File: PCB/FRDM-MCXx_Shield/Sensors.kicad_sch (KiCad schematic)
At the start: 3 parts, among them IC1 FXLS8974CF, J1 Conn_01x05_Socket

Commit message: Updated schematic
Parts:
- removed IC1: FXLS8974CF, FXLS8974CF, symbol SamacSys_Parts:FXLS8974CF
- added C10, C12, C8: 100nF, Capacitor_SMD:C_0603_1608Metric_Pad1.08x0.95mm_HandSolder, symbol Device:C
- added C11: 1uF, Capacitor_SMD:C_0603_1608Metric_Pad1.08x0.95mm_HandSolder, symbol Device:C
- added RN2: 4.7k, Resistor_SMD:R_Array_Convex_4x0603, symbol Device:R_Pack04_Split
- added U4: FXLS8974CF, FXLS8974CF, symbol SamacSys_Parts:FXLS8974CF
- added U5: SHT31A-DIS, Sensor_Humidity:Sensirion_DFN-8-1EP_2.5x2.5mm_P0.5mm_EP1.1x1.7mm, symbol Sensor_Humidity:SHT31A-DIS
- J1: footprint (none) -> Connector_PinHeader_2.54mm:PinHeader_1x05_P2.54mm_Vertical
- RV1: value R_Potentiometer -> 5k; footprint (none) -> Potentiometer_THT:Potentiometer_Vishay_T73YP_Vertical
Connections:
- net +3.3V: now also RV1.1, C10.1, C11.1, C12.2, C8.1, RN2.7 (R2.2), RN2.8 (R1.2), U4.1 (VDD), U4.9 (INTF_SEL), U5.5 (VDD)
- net GND: now also RV1.3, C10.2, C11.2, C12.1, C8.2, U4.10 (GND), U4.2 (BT_MODE), U5.2 (ADDR), U5.7 (R), U5.8 (VSS), U5.9 (VSS)
- net ADC_OUT: now reaches RV1.2
- new net ACEL_CS: U4.7 (SPI_CS_B/WAKE_UP)
- new net ACEL_INT1: RN2.1 (R1.1), U4.8 (INT1/MOT_DET)
- new net ACEL_INT2: RN2.2 (R2.1), U4.6 (INT2/EXT_TRIG/BOOT_OUT)
- new net SCL: U5.4 (SCL)
- new net SDA: U5.1 (SDA)
- new net SPI_CLK: U4.5 (SCL/SCLK)
- new net SPI_MISO: U4.3 (SA0/SPI_MISO)
- new net SPI_MOSI: U4.4 (SDA/SPI_MOSI/SPI_DATA)
- new net TEMP_ALERT: U5.3 (ALERT)
- new net ~{TEMP_RST}: U5.6 (~{RESET})
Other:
- company: (none) -> HAN
- title: (none) -> Sensors
- moved on the sheet: RV1

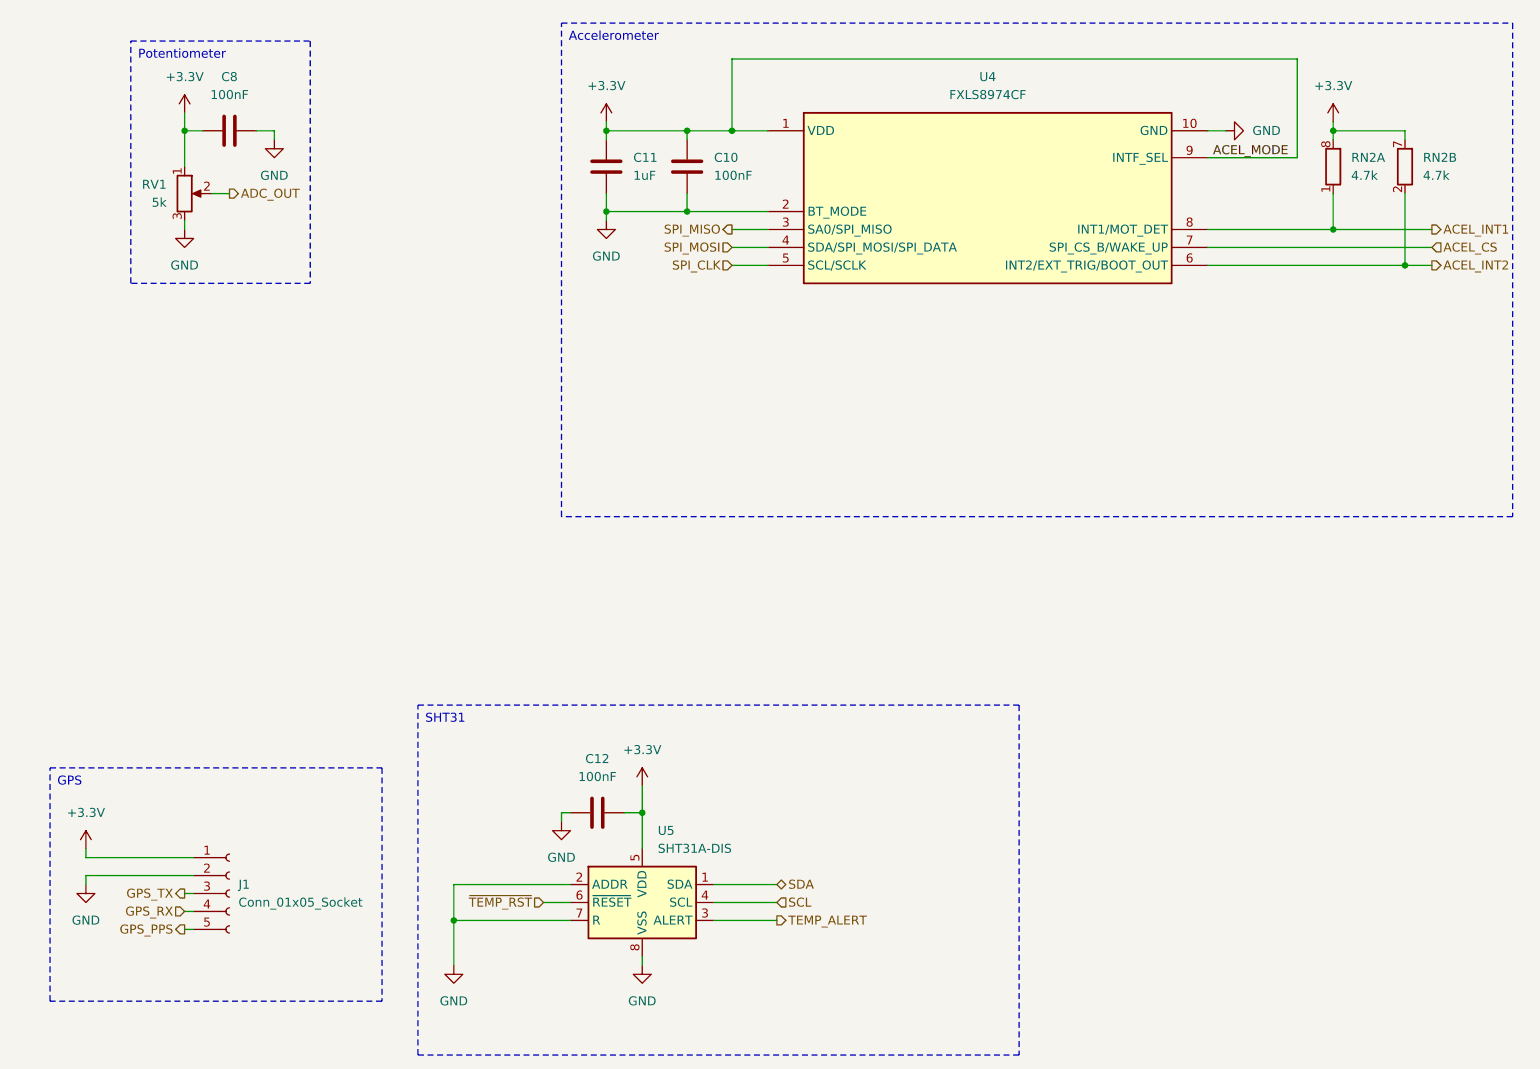
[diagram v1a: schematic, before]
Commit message: Update schematic and footprint
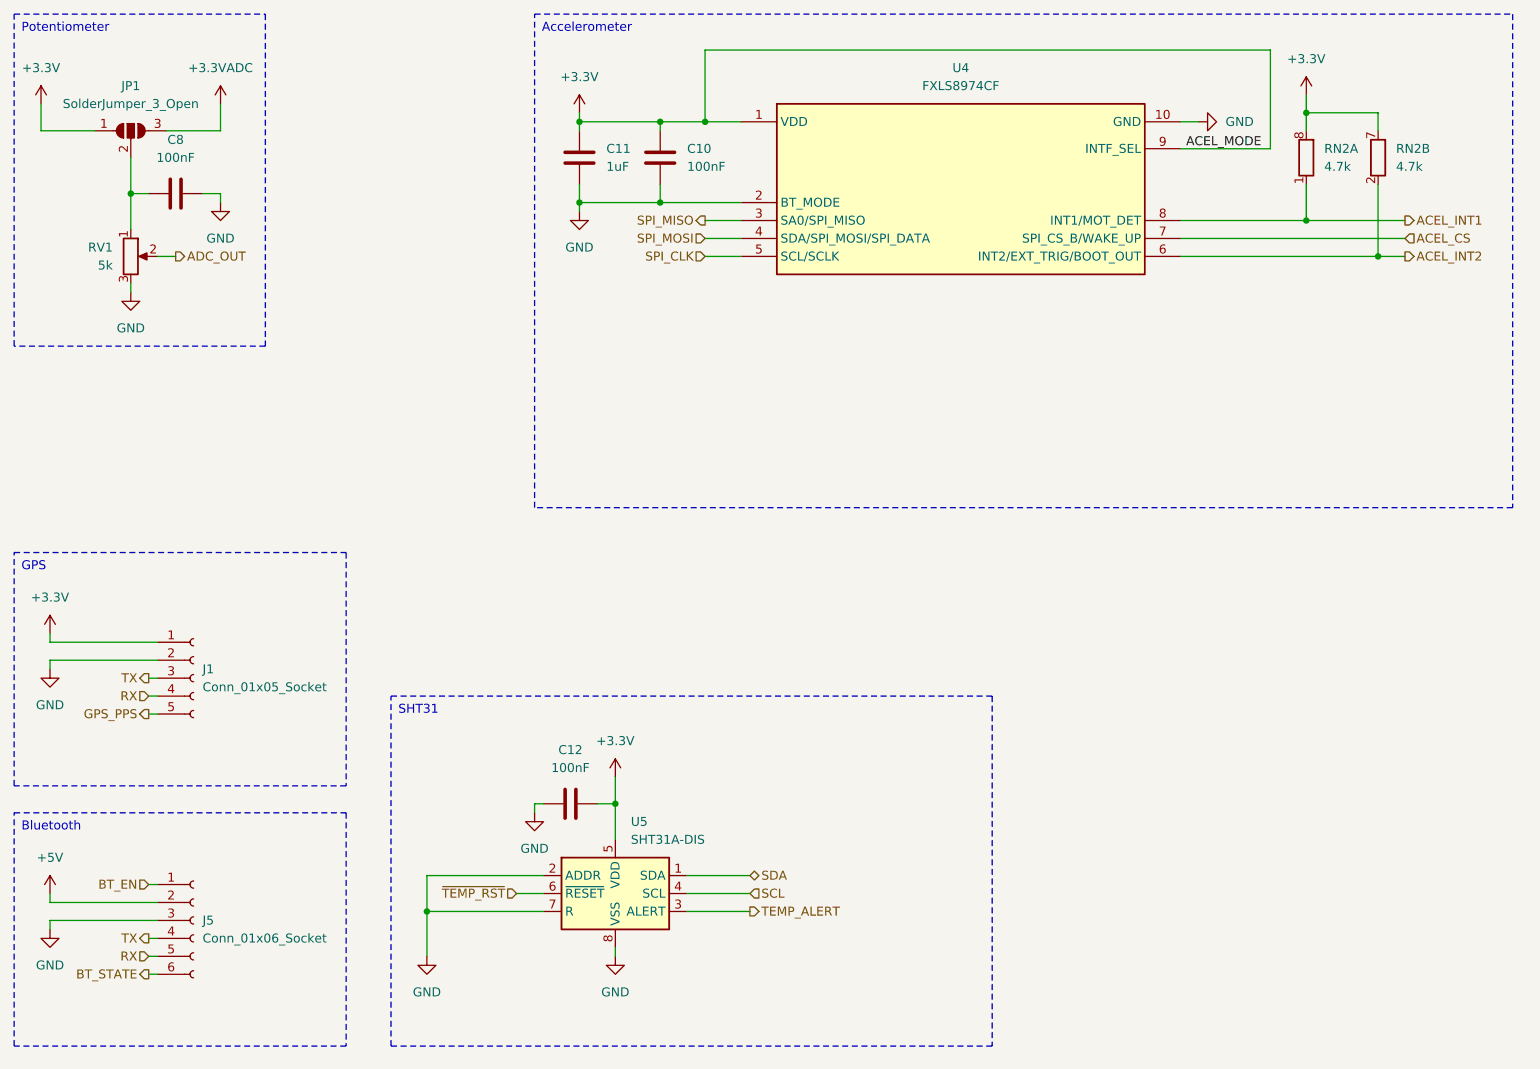
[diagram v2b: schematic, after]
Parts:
- added J5: Conn_01x06_Socket, Connector_PinHeader_2.54mm:PinHeader_1x06_P2.54mm_Vertical, symbol Connector:Conn_01x06_Socket
- added JP1: SolderJumper_3_Open, Jumper:SolderJumper-3_P2.0mm_Open_TrianglePad1.0x1.5mm_NumberLabels, symbol Jumper:SolderJumper_3_Open
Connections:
- net +3.3V: now also JP1.1 (A); no longer C8.1, RV1.1
- net GND: now also J5.3 (Pin_3)
- net GPS_RX renamed RX
- net RX: now also J5.5 (Pin_5)
- net GPS_TX renamed TX
- net TX: now also J5.4 (Pin_4)
- new net: C8.1, JP1.2 (C), RV1.1
- new net +3.3VADC: JP1.3 (B)
- new net +5V: J5.2 (Pin_2)
- new net BT_EN: J5.1 (Pin_1)
- new net BT_STATE: J5.6 (Pin_6)
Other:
- moved on the sheet: C10, C11, C12, C8, J1, RN2A, RN2B, RV1, U4, U5

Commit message: Updated schematic and PCB
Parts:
- RV1: footprint Potentiometer_THT:Potentiometer_Vishay_T73YP_Vertical -> Potentiometer_THT:Potentiometer_Bourns_3386P_Vertical
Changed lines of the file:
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@@
       (effects (font (size 1.27 1.27)) (justify right))
     )
-    (property "Footprint" "Potentiometer_THT:Potentiometer_Vishay_T73YP_Vertical" (at 49.53 71.12 0)
+    (property "Footprint" "Potentiometer_THT:Potentiometer_Bourns_3386P_Vertical" (at 49.53 71.12 0)
       (effects (font (size 1.27 1.27)) hide)
     )

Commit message: Updated schematic and PCB files
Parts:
- J4: renamed from J1; footprint Connector_PinHeader_2.54mm:PinHeader_1x05_P2.54mm_Vertical -> Connector_PinSocket_2.54mm:PinSocket_1x05_P2.54mm_Vertical
- J5: footprint Connector_PinHeader_2.54mm:PinHeader_1x06_P2.54mm_Vertical -> Connector_PinSocket_2.54mm:PinSocket_1x06_P2.54mm_Vertical
- renumbered C11 to C6, C10 to C7, C12 to C9, U4 to U2, U5 to U3
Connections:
- net +3.3V: now also JP1.3 (B); no longer JP1.1 (A)
- net +3.3VADC: now also JP1.1 (A); no longer JP1.3 (B)

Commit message: Updated PCB
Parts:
- added Brd1: SSD1306, OLED:128x64OLED, symbol OLED:SSD1306
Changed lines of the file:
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@@
+    )
+  )
+  (symbol (lib_id "OLED:SSD1306") (at 109.22 124.46 0) (unit 1)
+    (in_bom yes) (on_board yes) (dnp no) (fields_autoplaced)
+    (property "Reference" "Brd1" (at 116.84 123.19 0)
+      (effects (font (size 1.27 1.27)) (justify left))
+    )
+    (property "Value" "SSD1306" (at 116.84 125.73 0)
+      (effects (font (size 1.27 1.27)) (justify left))
+    )
+    (property "Footprint" "OLED:128x64OLED" (at 109.22 118.11 0)
+      (effects (font (size 1.27 1.27)) hide)
+    )
+    (property "Datasheet" "" (at 109.22 118.11 0)
+      (effects (font (size 1.27 1.27)) hide)
+    )
+    (pin "2")
+    (pin "3")
+    (pin "1")
+    (pin "4")
+    (instances
+      (project "FRDM-MCXx_Shield"
+        (path "/bffc27af-f9e0-4cc8-b5dc-88d2faf26a17/1dfdf8f6-c624-48d2-b647-f547c6376b37"
+          (reference "Brd1") (unit 1)
+        )
+      )
     )
   )

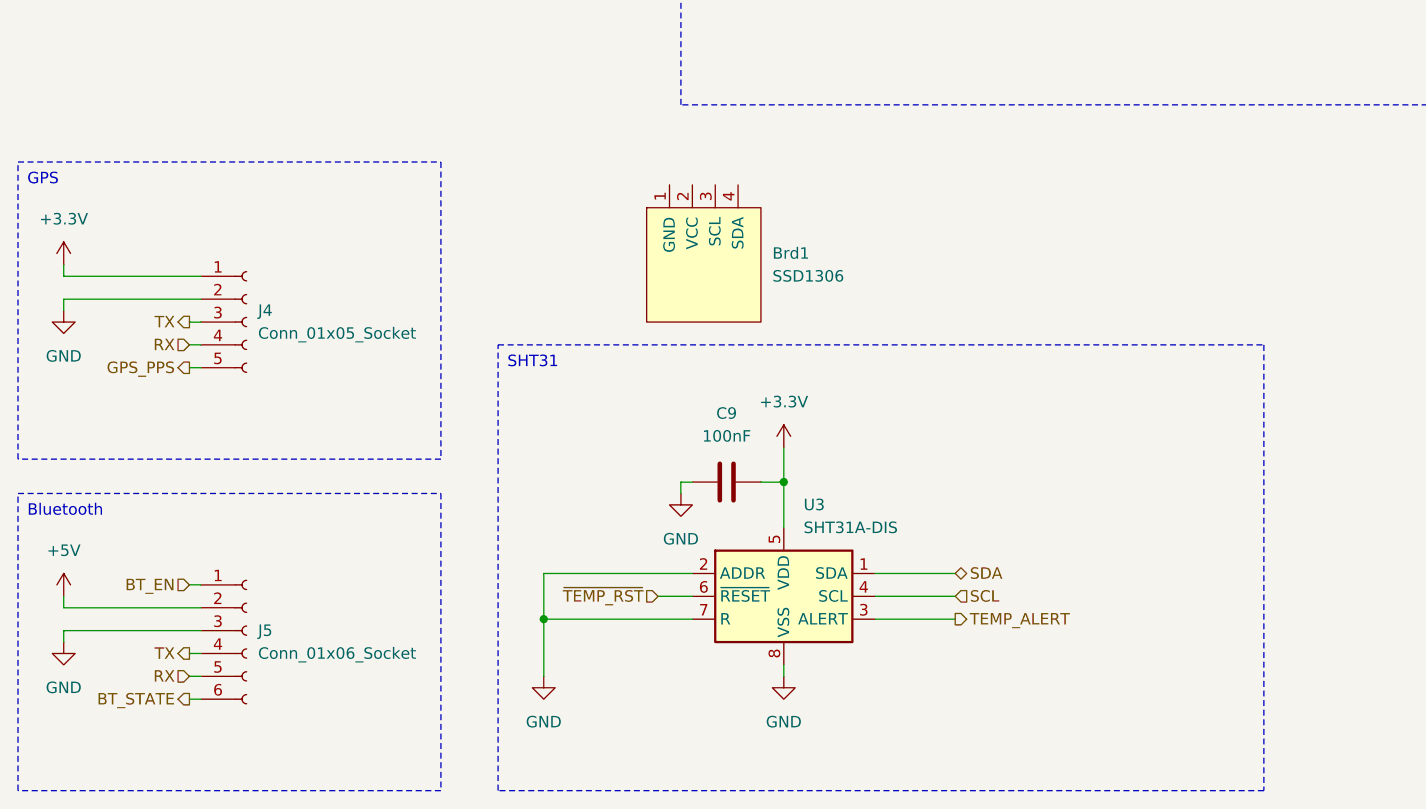
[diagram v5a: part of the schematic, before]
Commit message: Updated schematic and PCB
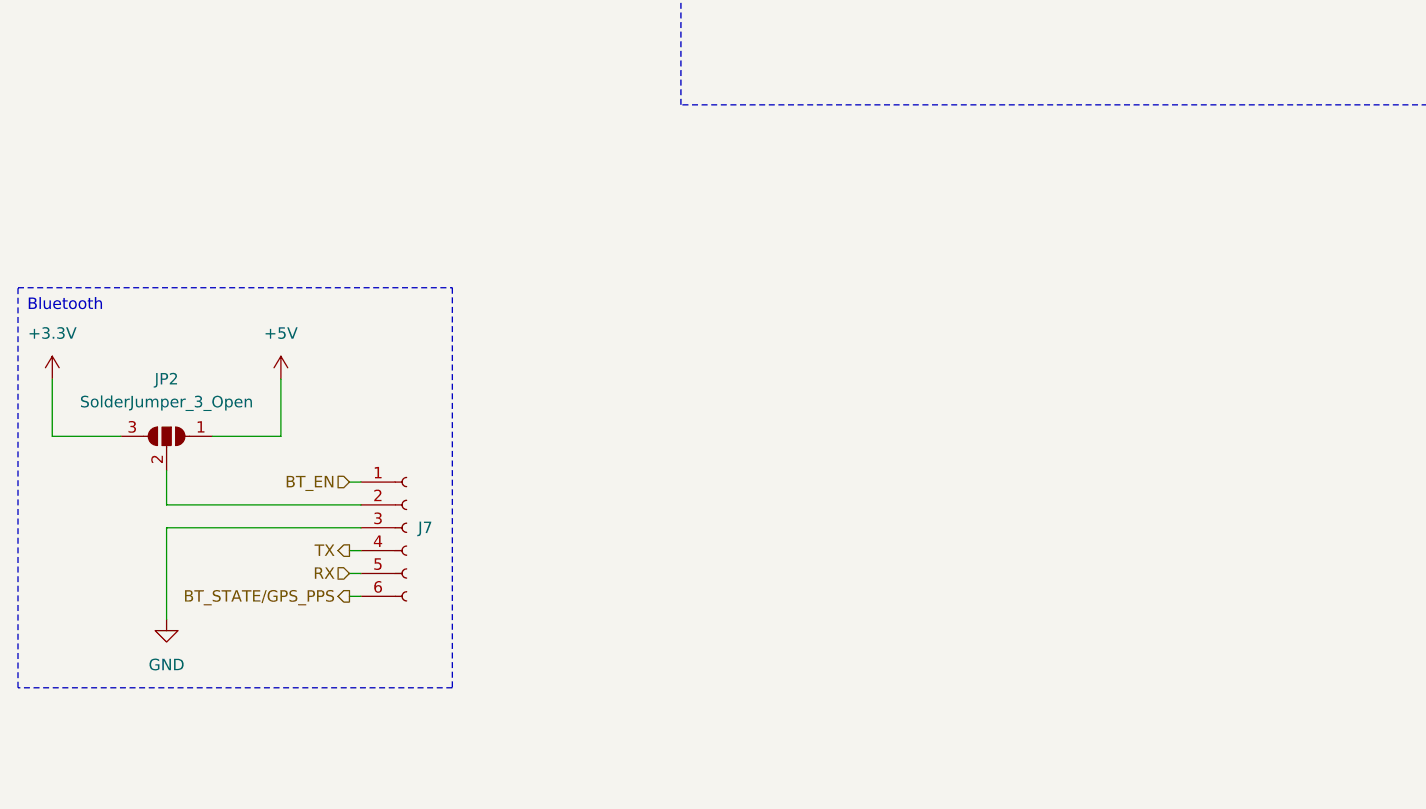
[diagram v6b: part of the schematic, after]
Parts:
- removed Brd1: SSD1306, OLED:128x64OLED, symbol OLED:SSD1306
- removed C9: 100nF, Capacitor_SMD:C_0603_1608Metric_Pad1.08x0.95mm_HandSolder, symbol Device:C
- removed J4: Conn_01x05_Socket, Connector_PinSocket_2.54mm:PinSocket_1x05_P2.54mm_Vertical, symbol Connector:Conn_01x05_Socket
- removed U3: SHT31A-DIS, Sensor_Humidity:Sensirion_DFN-8-1EP_2.5x2.5mm_P0.5mm_EP1.1x1.7mm, symbol Sensor_Humidity:SHT31A-DIS
- added JP2: SolderJumper_3_Open, Connector_PinHeader_2.54mm:PinHeader_1x03_P2.54mm_Vertical, symbol Jumper:SolderJumper_3_Open
- JP1: footprint Jumper:SolderJumper-3_P2.0mm_Open_TrianglePad1.0x1.5mm_NumberLabels -> Connector_PinHeader_2.54mm:PinHeader_1x03_P2.54mm_Vertical
- renumbered J5 to J7
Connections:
- net +3.3V: now also JP2.3 (B)
- net +5V: now also JP2.1 (A); no longer J7.2 (Pin_2)
- net BT_STATE renamed BT_STATE/GPS_PPS
- new net: J7.2 (Pin_2), JP2.2 (C)
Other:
- moved on the sheet: J7
